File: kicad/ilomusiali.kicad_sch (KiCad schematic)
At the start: 82 parts, among them J1 FPC/0.5mm/bottom contact, J2 2.54mmTestPoints, J3 SHOUNAN-MICRO180JB, Q1 AO3400A, Q2 AO3400A, Q3 AO3400A, SW1 SW_Push, SW10 SW_Push, SW11 SW_Push, SW12 SW_Push, SW13 SW_Push, SW14 SW_Push, SW15 SW_Push, SW16 SW_Push, SW17 SW_Push, SW18 SW_SPDT, SW2 SW_Push, SW3 SW_Push, SW4 SW_Push, SW5 SW_Push, SW6 SW_Push, SW7 SW_Push, SW8 SW_Push, SW9 SW_Push, U1 CH32V006F8U6, U2 NB25Q40BTIGT, U3 TX4310B, Y1 24M/CL=12pf

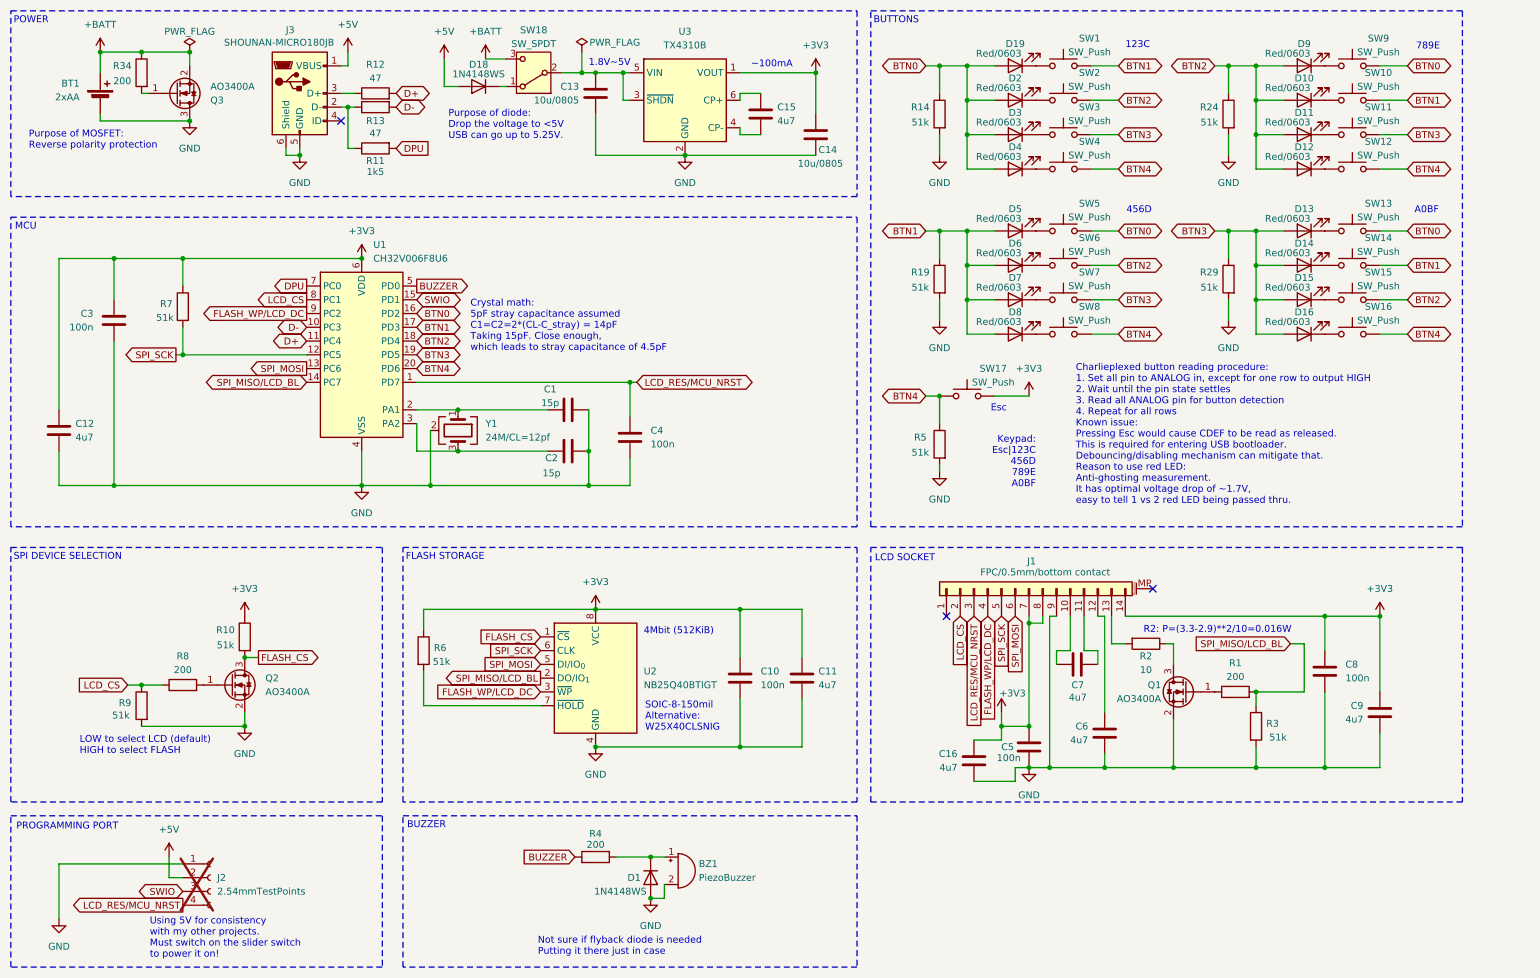
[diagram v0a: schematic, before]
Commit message: electronics: Fixed a few bugs, including battery polarity protection bug, using a better diode, lowered USB serial resistor's value and fixed potential short circuit condition in case the Esc button is pressed; Also added documentations
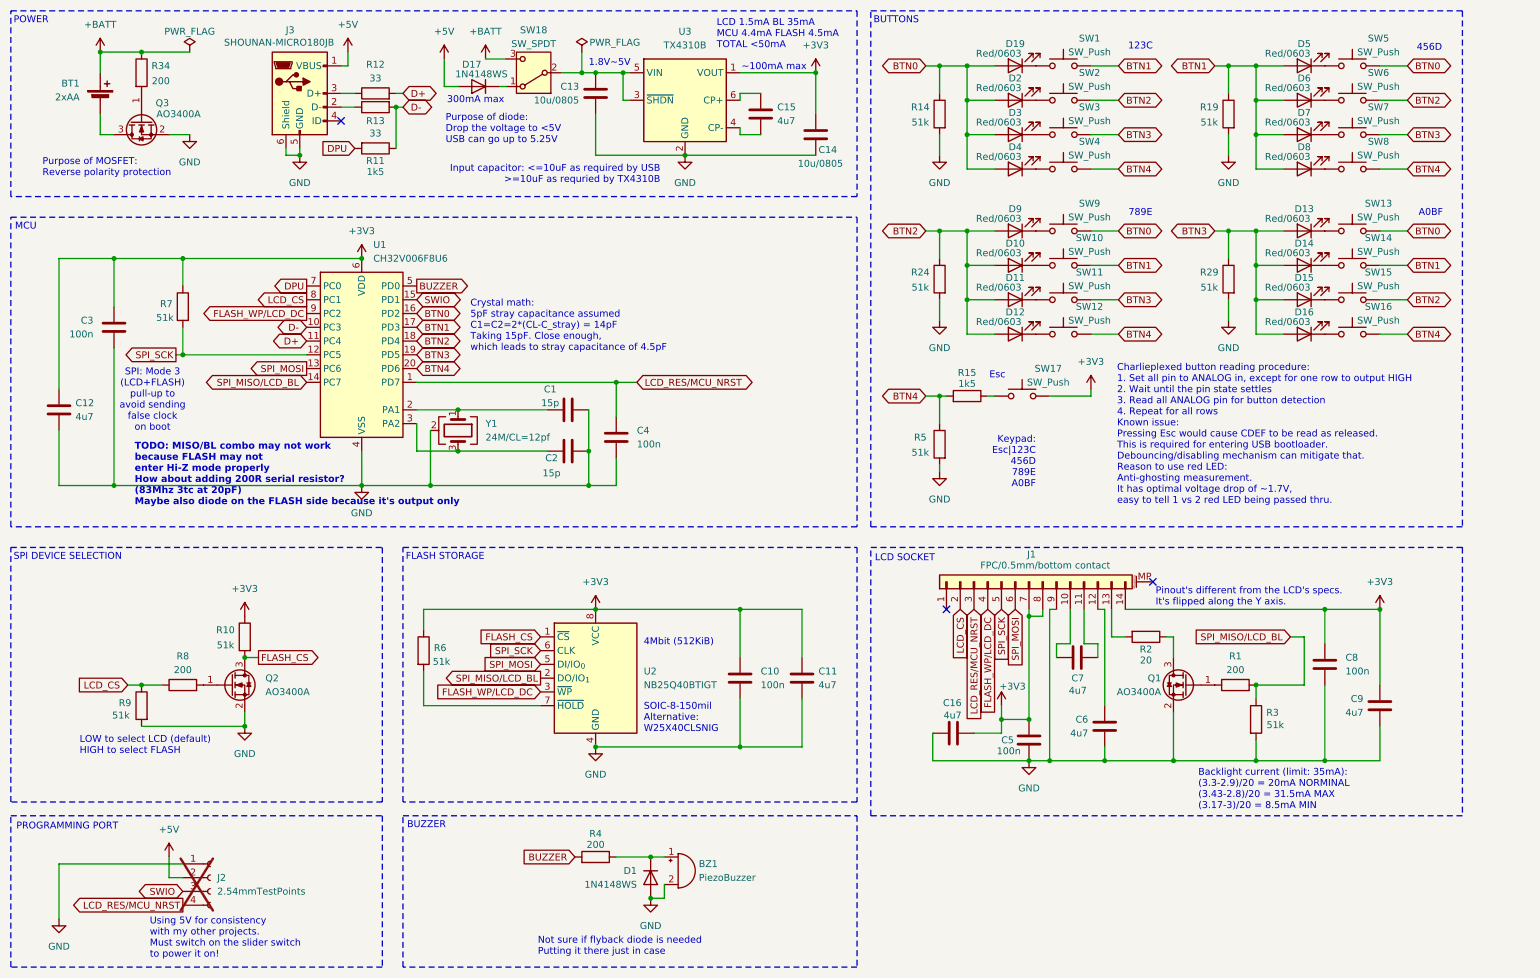
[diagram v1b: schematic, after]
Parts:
- removed D18: 1N4148WS, Diode_SMD:D_SOD-323, symbol Diode:1N4148WS
- added D17: 1N4148WS, Diode_SMD:D_SOD-323, symbol Diode:1N4148WS
- added R15: 1k5, symbol Device:R
- R12, R13: value 47 -> 33
- R2: value 10 -> 20
- Y1: LCSC C70590 -> C362340
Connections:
- net +3V3: now also C16.2; no longer C16.1
- net +5V: now also D17.2 (A)
- net +BATT: no longer Q3.2 (S)
- net BTN4: now also R15.2; no longer SW17.1
- net D-: now also R11.1
- net GND: now also C16.1, Q3.2 (S); no longer BT1.2 (-), C16.2, Q3.3 (D)
- net at J3.2 (D-), R13.1: no longer R11.1
- net at SW18.1 (A): now also D17.1 (K)
- new net: BT1.2 (-), Q3.3 (D)
- new net: R15.1, SW17.1
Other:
- note added: "300mA max"
- note added: "Backlight current (limit: 35mA): (3.3-2.9)/20 = 20mA NORMINAL (3.43-2.8)/20 = 31.5mA MAX (3.17-3)/20 = 8.5mA MIN"
- note added: "Input capacitor: <=10uF as required by USB >=10uF as requried by TX4310B"
- note added: "LCD 1.5mA BL 35mA MCU 4.4mA FLASH 4.5mA TOTAL <50mA"
- note added: "Pinout's different from the LCD's specs. It's flipped along the Y axis."
- note added: "Purpose of diode: Drop the voltage to <5V USB can go up to 5.25V"
- note added: "SPI: Mode 3 (LCD+FLASH) pull-up to avoid sending false clock on boot"
- note added: "TODO: MISO/BL combo may not work because FLASH may not enter Hi-Z mode properly How about adding 200R serial resistor? (83Mhz 3tc at 20pF) Maybe also diode on the FLASH side because it's output only"
- note added: "~100mA max"
- note removed: "Purpose of diode: Drop the voltage to <5V USB can go up to 5.25V."
- note removed: "R2: P=(3.3-2.9)**2/10=0.016W"
- note removed: "~100mA"
- moved on the sheet: C12, C16, C3, C4, C5, C6, C7, C8, C9, D10, D11, D12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

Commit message: electronics: Made first draft of component placement
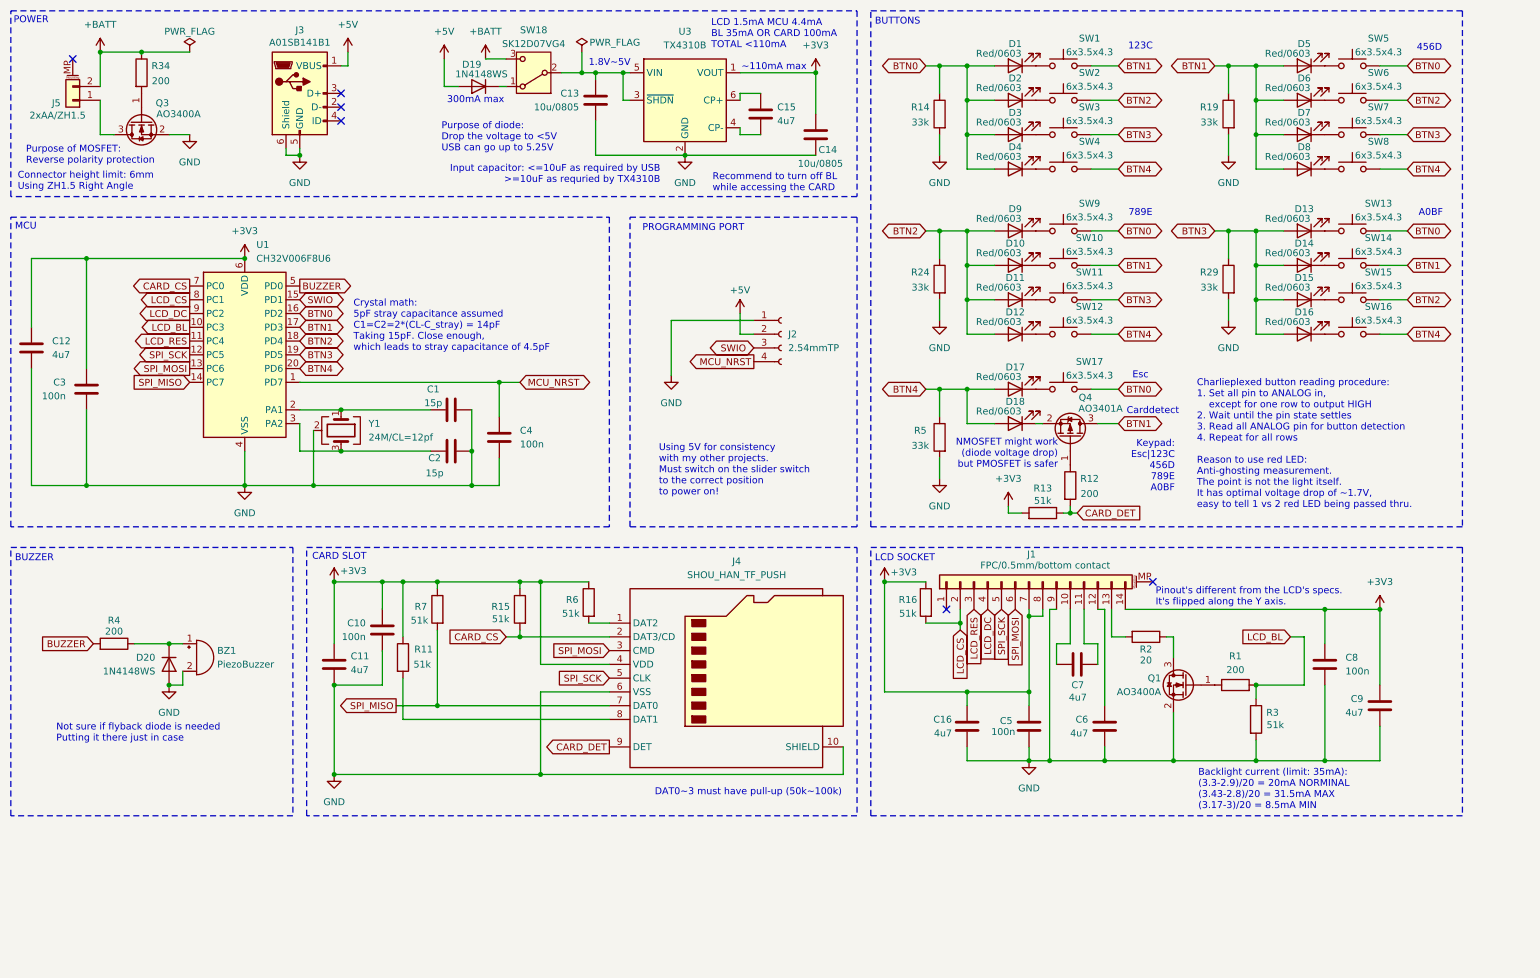
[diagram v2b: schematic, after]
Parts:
- removed BT1: 2xAA, symbol Device:Battery_Cell
- removed Q2: AO3400A, Package_TO_SOT_SMD:SOT-23, symbol Transistor_FET:AO3400A
- removed R10, R9: 51k, symbol Device:R
- removed R8: 200, symbol Device:R
- removed U2: NB25Q40BTIGT, Package_SO:SOIC-8_3.9x4.9mm_P1.27mm, symbol Memory_Flash:W25X40CLSN
- added D17, D18: Red/0603, LED_SMD:LED_0603_1608Metric, symbol Device:LED
- added J4: SHOU_HAN_TF_PUSH, project_components:SHOU_HAN_TF_PUSH, symbol Connector:Micro_SD_Card_Det1
- added J5: 2xAA/ZH1.5, Connector_JST:JST_ZH_S2B-ZR-SM4A-TF_1x02-1MP_P1.50mm_Horizontal, symbol Connector_Generic_MountingPin:Conn_01x02_MountingPin
- added Q4: AO3401A, Package_TO_SOT_SMD:SOT-23, symbol Transistor_FET:AO3401A
- added R16: 51k, Resistor_SMD:R_0603_1608Metric, symbol Device:R
- BZ1: footprint (none) -> Connector_Wire:SolderWire-0.1sqmm_1x02_P3.6mm_D0.4mm_OD1mm_Relief; now left out of the parts list
- C1, C2: footprint (none) -> Capacitor_SMD:C_0603_1608Metric
- C10, C3, C4, C5, C8: footprint (none) -> Capacitor_SMD:C_0603_1608Metric; LCSC (none) -> C14663
- C11, C12, C15, C16, C6, C7, C9: footprint (none) -> Capacitor_SMD:C_0603_1608Metric; LCSC (none) -> C19666
- C13, C14: footprint (none) -> Capacitor_SMD:C_0805_2012Metric; LCSC (none) -> C15850
- D1: renamed from D19; footprint (none) -> LED_SMD:LED_0603_1608Metric; LCSC (none) -> C2286
- D10, D11, D12, D13, D14, D15, D16, D2, D3, D4, D5, D6, D7, D8, D9: footprint (none) -> LED_SMD:LED_0603_1608Metric; LCSC (none) -> C2286
- D19: renamed from D17; footprint Diode_SMD:D_SOD-323 -> project_components:D_SOD-323_LargePads; LCSC (none) -> C2128
- D20: renamed from D1; footprint Diode_SMD:D_SOD-323 -> project_components:D_SOD-323_LargePads; LCSC (none) -> C2128
- J1: footprint (none) -> project_components:Jushuo_AFC01-S14FCx-00_14P_P0.50mm_Horizontal; LCSC C2856818 -> C577443
- J2: value 2.54mmTestPoints -> 2.54mmTP; footprint (none) -> Connector_PinHeader_2.54mm:PinHeader_1x04_P2.54mm_Vertical; now fitted; now left out of the parts list
- J3: value SHOUNAN-MICRO180JB -> A01SB141B1; footprint (none) -> project_components:USB_Micro-B_A01SB141B1-067; LCSC C456007 -> C404969
- Q1, Q3: LCSC (none) -> C20917
- R1, R34, R4: footprint (none) -> Resistor_SMD:R_0603_1608Metric; LCSC (none) -> C8218
- R11, R15: value 1k5 -> 51k; footprint (none) -> Resistor_SMD:R_0603_1608Metric; LCSC (none) -> C23196
- R12: value 33 -> 200; footprint (none) -> Resistor_SMD:R_0603_1608Metric; LCSC (none) -> C8218
- R13: value 33 -> 51k; footprint (none) -> Resistor_SMD:R_0603_1608Metric; LCSC (none) -> C23196
- R14, R19, R24, R29, R5: value 51k -> 33k; footprint (none) -> Resistor_SMD:R_0603_1608Metric; LCSC (none) -> C4216
- R2: footprint (none) -> Resistor_SMD:R_0603_1608Metric; LCSC (none) -> C22950
- R3, R6, R7: footprint (none) -> Resistor_SMD:R_0603_1608Metric; LCSC (none) -> C23196
- SW1, SW10, SW11, SW12, SW13, SW14, SW15, SW16, SW17, SW2, SW3, SW4, SW5, SW6, SW7, SW8, SW9: value SW_Push -> 6x3.5x4.3; footprint (none) -> project_components:ZX-QC36-4.3TPWD; LCSC (none) -> C7470221
- SW18: value SW_SPDT -> SK12D07VG4; footprint (none) -> Button_Switch_THT:SW_Slide_SPDT_Angled_CK_OS102011MA1Q; LCSC (none) -> C393937
- U1: footprint Package_DFN_QFN:QFN-20-1EP_3x3mm_P0.4mm_EP1.65x1.65mm -> Package_DFN_QFN:QFN-20-1EP_3x3mm_P0.4mm_EP1.65x1.65mm_ThermalVias
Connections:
- net +3V3: now also R11.1, R13.2, R15.1, J4.4 (VDD), R16.1; no longer SW17.2
- net +BATT: now also J5.2 (Pin_2)
- net BTN0: now also SW17.2
- net BTN1: now also Q4.3 (D)
- net BTN4: now also D17.2 (A), D18.2 (A); no longer R15.2
- net GND: now also J4.10 (SHIELD), J4.6 (VSS)
- net LCD_CS: now also R16.2
- net SPI_MOSI: now also J4.3 (CMD)
- net SPI_SCK: now also J4.5 (CLK); no longer R7.2
- net at R6.2: now also J4.1 (DAT2)
- net at J3.2 (D-): no longer R13.1
- net at Q3.3 (D): now also J5.1 (Pin_1)
- net at R12.1: now also Q4.1 (G); no longer J3.3 (D+)
- net at SW17.1: now also D17.1 (K); no longer R15.1
- net D+ renamed CARD_DET
- net CARD_DET: now also R13.1, J4.9 (DET); no longer U1.11 (PC4)
- removed net D-: R11.1, R13.2, U1.10 (PC3)
- net DPU: no longer names the net of R11.2
- net DPU: now also J4.8 (DAT1); no longer U1.7 (PC0)
- net FLASH_WP/LCD_DC renamed LCD_DC
- net LCD_RES/MCU_NRST renamed MCU_NRST
- net MCU_NRST: no longer J1.3 (Pin_3)
- net SPI_MISO/LCD_BL renamed LCD_BL
- net LCD_BL: now also U1.10 (PC3); no longer U1.14 (PC7)
- new net: D18.1 (K), Q4.2 (S)
- new net CARD_CS: J4.2 (DAT3/CD), R15.2, U1.7 (PC0)
- new net LCD_RES: J1.3 (Pin_3), U1.11 (PC4)
- new net SPI_MISO: J4.7 (DAT0), R7.2, U1.14 (PC7)
- no-connect marks 3 -> 6
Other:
- note added: "CARD SLOT"
- note added: "Carddetect"
- note added: "Charlieplexed button reading procedure: 1. Set all pin to ANALOG in, except for one row to output HIGH 2. Wait until the pin state settles 3. Read all ANALOG pin for button detection 4. Repeat for all rows Reason to use red LED: Anti-ghosting measurement. The point is not the light itself. It has optimal voltage drop of ~1.7V, easy to tell 1 vs 2 red LED being passed thru."
- note added: "Connector height limit: 6mm Using ZH1.5 Right Angle"
- note added: "DAT0~3 must have pull-up (50k~100k)"
- note added: "LCD 1.5mA MCU 4.4mA BL 35mA OR CARD 100mA TOTAL <110mA"
- note added: "NMOSFET might work (diode voltage drop) but PMOSFET is safer"
- note added: "Recommend to turn off BL while accessing the CARD"
- note added: "Using 5V for consistency with my other projects. Must switch on the slider switch to the correct position to power on!"
- note added: "~110mA max"
- note removed: "4Mbit (512KiB)"
- note removed: "Charlieplexed button reading procedure: 1. Set all pin to ANALOG in, except for one row to output HIGH 2. Wait until the pin state settles 3. Read all ANALOG pin for button detection 4. Repeat for all rows Known issue: Pressing Esc would cause CDEF to be read as released. This is required for entering USB bootloader. Debouncing/disabling mechanism can mitigate that. Reason to use red LED: Anti-gh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"
- note removed: "FLASH STORAGE"
- note removed: "LCD 1.5mA BL 35mA MCU 4.4mA FLASH 4.5mA TOTAL <50mA"
- note removed: "LOW to select LCD (default) HIGH to select FLASH"
- note removed: "SOIC-8-150mil Alternative: W25X40CLSNIG"
- note removed: "SPI DEVICE SELECTION"
- note removed: "SPI: Mode 3 (LCD+FLASH) pull-up to avoid sending false clock on boot"
- note removed: "TODO: MISO/BL combo may not work because FLASH may not enter Hi-Z mode properly How about adding 200R serial resistor? (83Mhz 3tc at 20pF) Maybe also diode on the FLASH side because it's output only"
- note removed: "Using 5V for consistency with my other projects. Must switch on the slider switch to power it on!"
- note removed: "~100mA max"
- moved on the sheet: BZ1, C1, C10, C11, C12, C13, C16, C2, C3, C4, C5, C7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

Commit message: electronics: Completed layout for PCB rev0
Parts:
- added NT1: NetTie_2, project_components:NetTie-2_SMD_Pad0.2mm, symbol Device:NetTie_2
- J1: FT Position Offset (none) -> 0.0,0.4445
- J3: FT Position Offset (none) -> 0.0,-0.254
- J4: FT Position Offset (none) -> 0.0,0.41275
- J5: FT Position Offset (none) -> 0.0,-0.2; FT Rotation Offset (none) -> 180
- Q1, Q3, Q4, U3: FT Rotation Offset (none) -> 180
- U1: footprint Package_DFN_QFN:QFN-20-1EP_3x3mm_P0.4mm_EP1.65x1.65mm_ThermalVias -> Package_DFN_QFN:QFN-20-1EP_3x3mm_P0.4mm_EP1.65x1.65mm; FT Rotation Offset (none) -> -90
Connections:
- net GND: now also NT1.1; no longer C1.1, C2.2, Y1.2 (G), Y1.4 (G)
- new net GND2: C1.1, C2.2, NT1.2, Y1.2 (G), Y1.4 (G)
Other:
- note added: "Keypad: X|123C 456D 789E A0BF"
- note added: "Using 5V for consistency with my other projects. Must slide the slider switch to the correct position to power on!"
- note removed: "Keypad: Esc|123C 456D 789E A0BF"
- note removed: "Using 5V for consistency with my other projects. Must switch on the slider switch to the correct position to power on!"
- moved on the sheet: BZ1, C10, C11, D20, J4, R11, R15, R4, R6, R7
